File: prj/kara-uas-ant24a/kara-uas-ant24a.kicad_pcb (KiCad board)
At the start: 2 copper layers, 201.5 x 6 mm, 3 parts

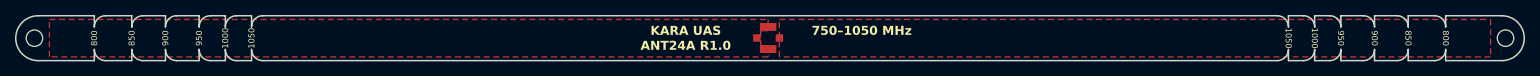
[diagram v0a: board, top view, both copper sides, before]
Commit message: Corrections to kara-uas-ant-24-a
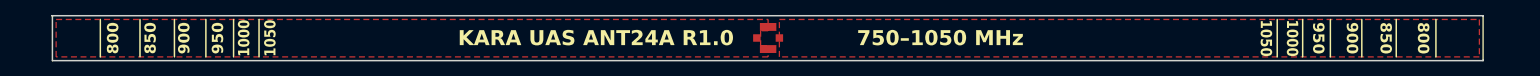
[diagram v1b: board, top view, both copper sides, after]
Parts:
- removed ? (x2): , 
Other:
- board size 201.5 x 6 mm -> 191.2 x 6 mm
- board text added: "KARA UAS ANT24A R1.0"
- board text removed: "ANT24A R1.0"
- board text removed: "KARA UAS"

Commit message: kara-uas-ant-24-a - center silkscreen frequency numbers
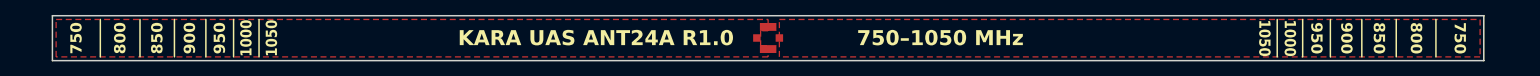
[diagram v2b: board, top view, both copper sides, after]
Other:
- outline, holes or cut-outs redrawn
- board text added: "750"
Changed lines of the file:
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@@
 			(fill solid)
 			(layer "F.Paste")
-			(net 3080250)
 		)
 		(fp_rect
@@
 			(fill solid)
 			(layer "F.Paste")
-			(net 3080250)
 		)
 		(fp_rect
@@
 			(fill solid)
 			(layer "F.Paste")
-			(net 3080250)
 		)
 		(fp_rect
@@
 			(fill solid)
 			(layer "F.Paste")
-			(net 3080250)
 		)
 		(fp_line
@@
 	)
 	(gr_line
-		(start 57.8 100.5)
-		(end 57.8 105.5)
+		(start 57.8 105.5)
+		(end 57.8 100.5)
 		(stroke
 			(width 0.2)
@@
 	)
 	(gr_line
-		(start 242.5 106)
-		(end 242.5 100)
+		(start 242.6 106)
+		(end 242.6 100)
 		(stroke
 			(width 0.2)
@@
 	(gr_line
 		(start 51.4 106)
-		(end 242.5 106)
+		(end 242.6 106)
 		(stroke
 			(width 0.2)
@@
 	)
 	(gr_line
-		(start 51.3 100)
-		(end 242.5 100)
+		(start 51.4 100)
+		(end 242.6 100)
 		(stroke
 			(width 0.2)
@@
 	)
 	(gr_text "900"
-		(at 225 103 -90)
+		(at 224.25 103 -90)
 		(layer "F.SilkS")
 		(effects
@@
 		)
 	)
+	(gr_text "750"
+		(at 54.6 103 90)
+		(layer "F.SilkS")
+		(effects
+			(font
+				(size 1.5 1.5)
+				(thickness 0.2)
+				(bold yes)
+			)
+		)
+	)
+	(gr_text "900"
+		(at 69.75 103 90)
+		(layer "F.SilkS")
+		(effects
+			(font
+				(size 1.5 1.5)
+				(thickness 0.2)
+				(bold yes)
+			)
+		)
+	)
+	(gr_text "750"
+		(at 239.4 102.999998 -90)
+		(layer "F.SilkS")
+		(effects
+			(font
+				(size 1.5 1.5)
+				(thickness 0.2)
+				(bold yes)
+			)
+		)
+	)
+	(gr_text "950"
+		(at 73.75 103 90)
+		(layer "F.SilkS")
+		(effects
+			(font
+				(size 1.5 1.5)
+				(thickness 0.2)
+				(bold yes)
+			)
+		)
+	)
+	(gr_text "1050"
+		(at 80.7 103 90)
+		(layer "F.SilkS")
+		(effects
+			(font
+				(size 1.5 1.3)
+				(thickness 0.2)
+				(bold yes)
+			)
+		)
+	)
+	(gr_text "950"
+		(at 220.25 103 -90)
+		(layer "F.SilkS")
+		(effects
+			(font
+				(size 1.5 1.5)
+				(thickness 0.2)
+				(bold yes)
+			)
+		)
+	)
+	(gr_text "1000"
+		(at 216.7 103 -90)
+		(layer "F.SilkS")
+		(effects
+			(font
+				(size 1.5 1.3)
+				(thickness 0.2)
+				(bold yes)
+			)
+		)
+	)
+	(gr_text "1000"
+		(at 77.3 103 90)
+		(layer "F.SilkS")
+		(effects
+			(font
+				(size 1.5 1.3)
+				(thickness 0.2)
+				(bold yes)
+			)
+		)
+	)
 	(gr_text "800"
-		(at 59.5 103 90)
+		(at 60.45 103 90)
 		(layer "F.SilkS")
 		(effects
@@
 		)
 	)
-	(gr_text "950"
-		(at 220.5 103 -90)
+	(gr_text "850"
+		(at 228.6 103 -90)
 		(layer "F.SilkS")
 		(effects
@@
 		)
 	)
-	(gr_text "1000"
-		(at 217 103 -90)
-		(layer "F.SilkS")
-		(effects
-			(font
-				(size 1.5 1.3)
-				(thickness 0.2)
-				(bold yes)
-			)
-		)
-	)
-	(gr_text "950"
-		(at 73.5 103 90)
+	(gr_text "850"
+		(at 65.4 103 90)
 		(layer "F.SilkS")
 		(effects
@@
 		)
 	)
-	(gr_text "850"
-		(at 64.5 103 90)
-		(layer "F.SilkS")
-		(effects
-			(font
-				(size 1.5 1.5)
-				(thickness 0.2)
-				(bold yes)
-			)
-		)
-	)
-	(gr_text "1050"
-		(at 80.5 103 90)
-		(layer "F.SilkS")
-		(effects
-			(font
-				(size 1.5 1.3)
-				(thickness 0.2)
-				(bold yes)
-			)
-		)
-	)
-	(gr_text "850"
-		(at 229.5 103 -90)
-		(layer "F.SilkS")
-		(effects
-			(font
-				(size 1.5 1.5)
-				(thickness 0.2)
-				(bold yes)
-			)
-		)
-	)
-	(gr_text "1000"
-		(at 77 103 90)
-		(layer "F.SilkS")
-		(effects
-			(font
-				(size 1.5 1.3)
-				(thickness 0.2)
-				(bold yes)
-			)
-		)
-	)
-	(gr_text "900"
-		(at 69 103 90)
-		(layer "F.SilkS")
-		(effects
-			(font
-				(size 1.5 1.5)
-				(thickness 0.2)
-				(bold yes)
-			)
-		)
-	)
 	(gr_text "800"
-		(at 234.5 103 -90)
+		(at 233.55 103 -90)
 		(layer "F.SilkS")
 		(effects
@@
 	)
 	(gr_text "1050"
-		(at 213.5 103 -90)
+		(at 213.3 103 -90)
 		(layer "F.SilkS")
 		(effects
@@
 		)
 		(height 11)
-		(gr_text "75.1000 mm"
+		(gr_text "75.1 mm"
 			(at 109.45 87.85 0)
 			(layer "Cmts.User")
@@
 			(units 3)
 			(units_format 1)
-			(precision 4)
+			(precision 1)
 		)
 		(style
@@
 		)
 		(height -6)
-		(gr_text "68.0000 mm"
+		(gr_text "68.0 mm"
 			(at 181 92.89825 0)
 			(layer "Cmts.User")
@@
 			(units 3)
 			(units_format 1)
-			(precision 4)
+			(precision 1)
 		)
 		(style
@@
 		)
 		(height -21)
-		(gr_text "95.1000 mm"
+		(gr_text "95.1 mm"
 			(at 194.55 77.89825 0)
 			(layer "Cmts.User")
@@
 			(units 3)
 			(units_format 1)
-			(precision 4)
+			(precision 1)
 		)
 		(style
@@
 		)
 		(height 8.5)
-		(gr_text "71.4000 mm"
+		(gr_text "71.4 mm"
 			(at 111.3 90.35 0)
 			(layer "Cmts.User")
@@
 			(units 3)
 			(units_format 1)
-			(precision 4)
+			(precision 1)
 		)
 		(style
@@
 		)
 		(height 18.5)
-		(gr_text "89.2000 mm"
+		(gr_text "89.2 mm"
 			(at 102.4 80.35 0)
 			(layer "Cmts.User")
@@
 			(units 3)
 			(units_format 1)
-			(precision 4)
+			(precision 1)
 		)
 		(style
@@
 		)
 		(height 6)
-		(gr_text "68.0000 mm"
+		(gr_text "68.0 mm"
 			(at 113 92.85 0)
 			(layer "Cmts.User")
@@
 			(units 3)
 			(units_format 1)
-			(precision 4)
+			(precision 1)
 		)
 		(style
@@
 		)
 		(height -18.5)
-		(gr_text "89.2000 mm"
+		(gr_text "89.2 mm"
 			(at 191.6 80.39825 0)
 			(layer "Cmts.User")
@@
 			(units 3)
 			(units_format 1)
-			(precision 4)
+			(precision 1)
 		)
 		(style
@@
 		)
 		(height -13.5)
-		(gr_text "79.3000 mm"
+		(gr_text "79.3 mm"
 			(at 186.65 85.39825 0)
 			(layer "Cmts.User")
@@
 			(units 3)
 			(units_format 1)
-			(precision 4)
+			(precision 1)
 		)
 		(style
@@
 		)
 		(height 16)
-		(gr_text "83.9000 mm"
+		(gr_text "83.9 mm"
 			(at 105.05 82.85 0)
 			(layer "Cmts.User")
@@
 			(units 3)
 			(units_format 1)
-			(precision 4)
+			(precision 1)
 		)
 		(style
@@
 		)
 		(height -16)
-		(gr_text "83.9000 mm"
+		(gr_text "83.9 mm"
 			(at 188.95 82.89825 0)
 			(layer "Cmts.User")
@@
 			(units 3)
 			(units_format 1)
-			(precision 4)
+			(precision 1)
 		)
 		(style
@@
 		)
 		(height -8.5)
-		(gr_text "71.4000 mm"
+		(gr_text "71.4 mm"
 			(at 182.7 90.39825 0)
 			(layer "Cmts.User")
@@
 			(units 3)
 			(units_format 1)
-			(precision 4)
+			(precision 1)
 		)
 		(style
@@
 		)
 		(height 13.5)
-		(gr_text "79.3000 mm"
+		(gr_text "79.3 mm"
 			(at 107.35 85.35 0)
 			(layer "Cmts.User")
@@
 			(units 3)
 			(units_format 1)
-			(precision 4)
+			(precision 1)
 		)
 		(style
@@
 		)
 		(height -11)
-		(gr_text "75.1000 mm"
+		(gr_text "75.1 mm"
 			(at 184.55 87.89825 0)
 			(layer "Cmts.User")
@@
 			(units 3)
 			(units_format 1)
-			(precision 4)
+			(precision 1)
 		)
 		(style
@@
 		)
 		(height 21)
-		(gr_text "95.1000 mm"
+		(gr_text "95.1 mm"
 			(at 99.45 77.85 0)
 			(layer "Cmts.User")
@@
 			(units 3)
 			(units_format 1)
-			(precision 4)
+			(precision 1)
 		)
 		(style
@@
 		(polygon
 			(pts
-				(xy 242 100.5) (xy 242 105.5) (xy 148.5 105.5) (xy 148.5 100.5)
-			)
-		)
+				(xy 242.1 100.5) (xy 242.1 105.5) (xy 148.5 105.5) (xy 148.5 100.5)
+			)
+		)
